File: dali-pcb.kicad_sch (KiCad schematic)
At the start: 6 parts

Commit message: Remove the kitchen sink
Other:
- sheet IO ports: added IO_D41, IO_D42; removed FTDI_MCU_RXD, FTDI_MCU_TXD
- sheet Microcontroller ports: added ESP32_GPIO41, ESP32_GPIO42; removed ESP32_U0RXD_GPIO44, ESP32_U0TXD_GPIO43, L_S3_MINI_GPIO38
- moved on the sheet: H1, H2, H3, H4

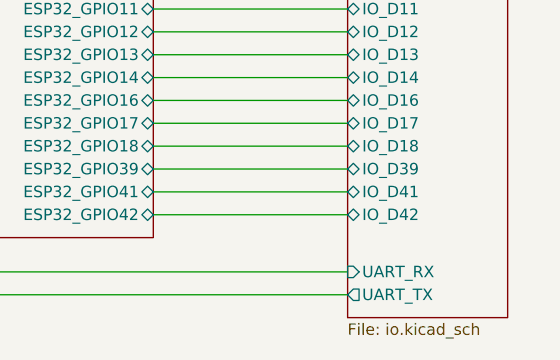
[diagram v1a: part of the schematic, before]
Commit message: Rename the UART connection to DIRECT because it needs Manchester encoding
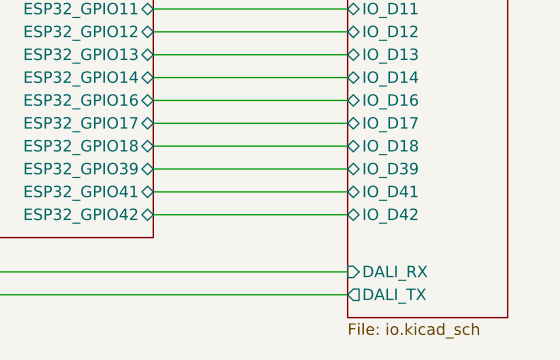
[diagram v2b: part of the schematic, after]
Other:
- sheet IO ports: added DALI_RX, DALI_TX; removed UART_RX, UART_TX
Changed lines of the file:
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@@
 			)
 		)
-		(pin "UART_RX" input
+		(pin "DALI_RX" input
 			(at 166.37 68.58 180)
 			(effects
@@
 			)
 		)
-		(pin "UART_TX" output
+		(pin "DALI_TX" output
 			(at 166.37 71.12 180)
 			(effects

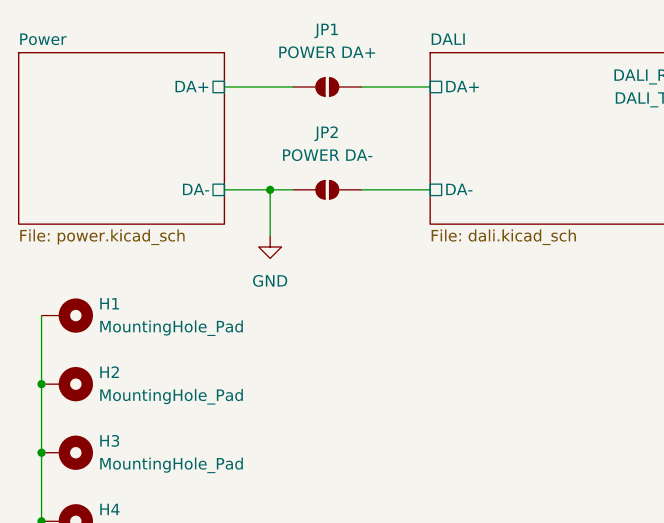
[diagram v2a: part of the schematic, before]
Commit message: Remove connection between J1 (1) and GND
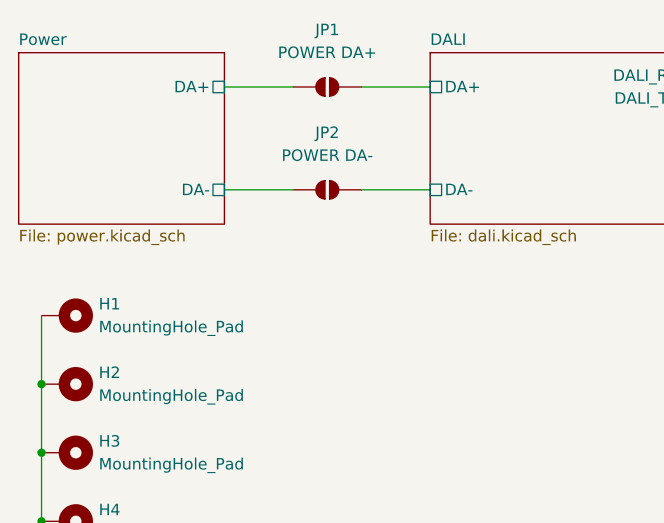
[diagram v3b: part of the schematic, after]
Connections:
- net GND: no longer JP2.1 (A)
- new net Power/DA-: JP2.1 (A)
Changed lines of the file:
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@@
-	)
-	(junction
-		(at 33.02 21.59)
-		(diameter 0)
-		(color 0 0 0 0)
 	)
 	(junction
@@
 	(wire
 		(pts
-			(xy 27.94 21.59) (xy 33.02 21.59)
+			(xy 27.94 21.59) (xy 35.56 21.59)
 		)
 		(stroke
@@
 	(wire
 		(pts
-			(xy 33.02 21.59) (xy 33.02 26.67)
-		)
-		(stroke
-			(width 0)
-			(type default)
-		)
-	)
-	(wire
-		(pts
 			(xy 91.44 11.43) (xy 91.44 71.12)
 		)
@@
 		(pts
 			(xy 43.18 10.16) (xy 50.8 10.16)
-		)
-		(stroke
-			(width 0)
-			(type default)
-		)
-	)
-	(wire
-		(pts
-			(xy 33.02 21.59) (xy 35.56 21.59)
 		)
 		(stroke
@@
 					(unit 1)
 				)
-			)
-		)
-	)
-	(symbol
-		(lib_id "power:GND")
-		(at 33.02 26.67 0)
-		(unit 1)
-		(exclude_from_sim no)
-		(in_bom yes)
-		(on_board yes)
-		(dnp no)
-		(fields_autoplaced yes)
-		(property "Reference" "#PWR08"
-			(at 33.02 33.02 0)
-			(effects
-				(font
-					(size 1.27 1.27)
-				)
-				(hide yes)
-			)
-		)
-		(property "Value" "GND"
-			(at 33.02 31.75 0)
-			(effects
-				(font
-					(size 1.27 1.27)
-				)
-			)
-		)
-		(property "Footprint" ""
-			(at 33.02 26.67 0)
-			(effects
-				(font
-					(size 1.27 1.27)
-				)
-				(hide yes)
-			)
-		)
-		(property "Datasheet" ""
-			(at 33.02 26.67 0)
-			(effects
-				(font
-					(size 1.27 1.27)
-				)
-				(hide yes)
-			)
-		)
-		(property "Description" "Power symbol creates a global label with name \"GND\" , ground"
-			(at 33.02 26.67 0)
-			(effects
-				(font
-					(size 1.27 1.27)
-				)
-				(hide yes)
-			)
-		)
-		(pin "1"
-		)
-		(instances
-			(project ""
-				(path "/aa7f7e07-1f39-4222-a272-c9975d033b6d"
-					(reference "#PWR08")
-					(unit 1)
-				)

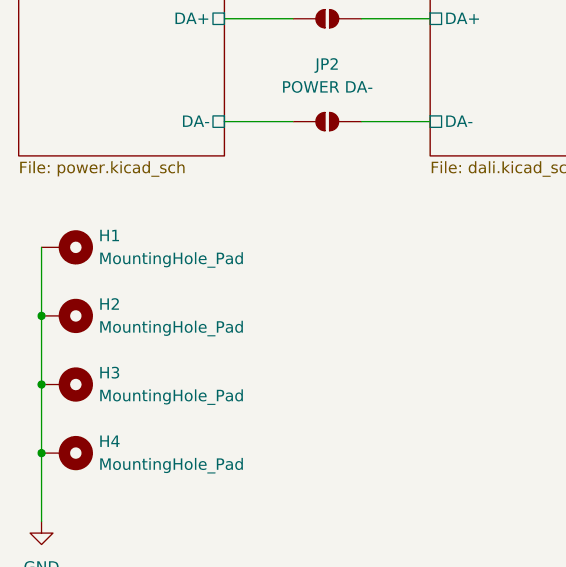
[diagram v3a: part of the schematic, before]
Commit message: Remove filled GND zone from under the DALI power/bus components
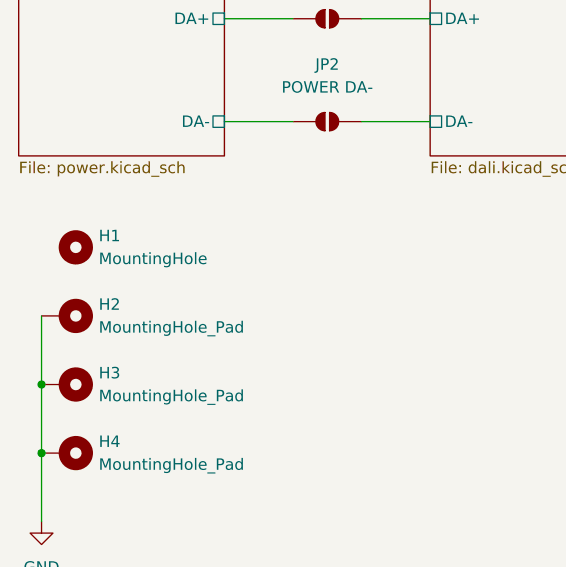
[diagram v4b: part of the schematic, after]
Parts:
- H1: value MountingHole_Pad -> MountingHole; footprint MountingHole:MountingHole_3.2mm_M3_Pad -> MountingHole:MountingHole_3.2mm_M3; symbol Mechanical:MountingHole_Pad -> Mechanical:MountingHole
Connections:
- net GND: no longer H1.1
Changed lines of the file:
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@@
-	)
-	(junction
-		(at 7.62 43.18)
-		(diameter 0)
-		(color 0 0 0 0)
 	)
 	(junction
@@
 		(pts
 			(xy 144.78 49.53) (xy 166.37 49.53)
-		)
-		(stroke
-			(width 0)
-			(type default)
-		)
-	)
-	(wire
-		(pts
-			(xy 7.62 35.56) (xy 7.62 43.18)
 		)
 		(stroke
@@
 	)
 	(symbol
-		(lib_id "Mechanical:MountingHole_Pad")
-		(at 10.16 35.56 270)
+		(lib_id "Mechanical:MountingHole")
+		(at 11.43 35.56 270)
 		(unit 1)
 		(exclude_from_sim no)
@@
 			)
 		)
-		(property "Value" "MountingHole_Pad"
+		(property "Value" "MountingHole"
 			(at 13.97 36.8299 90)
 			(effects
@@
 			)
 		)
-		(property "Footprint" "MountingHole:MountingHole_3.2mm_M3_Pad"
-			(at 10.16 35.56 0)
+		(property "Footprint" "MountingHole:MountingHole_3.2mm_M3"
+			(at 11.43 35.56 0)
 			(effects
 				(font
@@
 		)
 		(property "Datasheet" "~"
-			(at 10.16 35.56 0)
-			(effects
-				(font
-					(size 1.27 1.27)
-				)
-				(hide yes)
-			)
-		)
-		(property "Description" "Mounting Hole with connection"
-			(at 10.16 35.56 0)
-			(effects
-				(font
-					(size 1.27 1.27)
-				)
-				(hide yes)
-			)
-		)
-		(pin "1"
+			(at 11.43 35.56 0)
+			(effects
+				(font
+					(size 1.27 1.27)
+				)
+				(hide yes)
+			)
+		)
+		(property "Description" "Mounting Hole without connection"
+			(at 11.43 35.56 0)
+			(effects
+				(font
+					(size 1.27 1.27)
+				)
+				(hide yes)
+			)
 		)
 		(instances
